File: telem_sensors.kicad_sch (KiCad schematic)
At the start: 29 parts, among them J4 Thermistor Molex, J6 Thermistor Molex, J8 SMA, U10 MAX-M10S, U4 LSM6DSRXTR, U5 MCP6L01x-xLT, U7 BMP585, U8 MCP6L01x-xLT

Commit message: Updated Schematics & finished rev2 layout. Routing left
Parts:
- removed C21, C32, C33: 100nF, Capacitor_SMD:C_0603_1608Metric, symbol Device:C
- added C23, C25, C29: 100nF, Capacitor_SMD:C_0603_1608Metric, symbol Device:C
- C22, C24, C26, C27, C28, C30: Voltage Rating (none) -> 10V
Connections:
- net +1V8: now also C30.1
- net +3V3: now also C28.1, C23.1, C29.1; no longer C30.1
- net PGND: now also C23.2, C25.2, C29.2
- net THERM2: now also C25.1; no longer C28.1

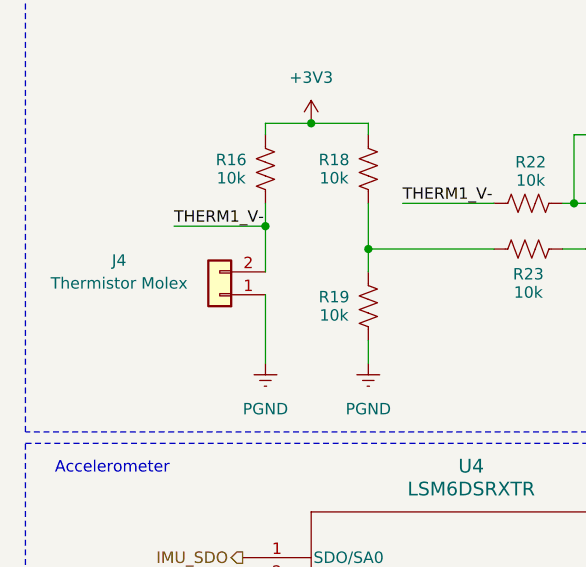
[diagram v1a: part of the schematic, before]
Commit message: Shrank board, updated all cap footprints. Updated thermistor headers to be vertical
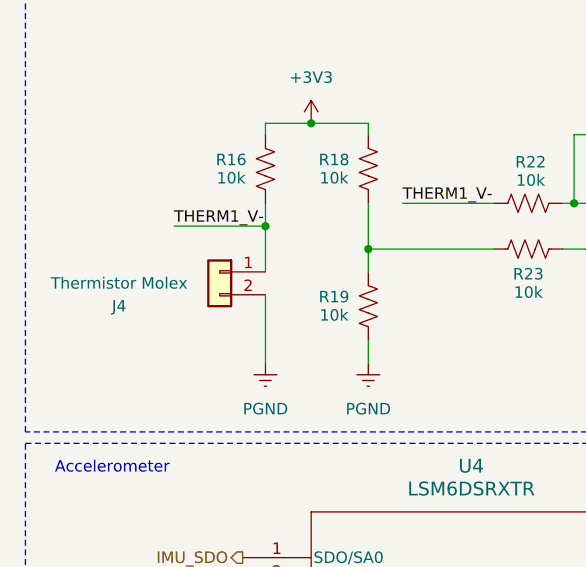
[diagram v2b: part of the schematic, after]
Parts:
- J4, J6: footprint Connector_Molex:Molex_MicroClasp_55935-0230_1x02_P2.00mm_Horizontal -> Connector_Molex:Molex_MicroClasp_55932-0230_1x02_P2.00mm_Vertical
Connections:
- net PGND: now also J4.2 (Pin_2); no longer J4.1 (Pin_1)
- net THERM1_V-: now also J4.1 (Pin_1); no longer J4.2 (Pin_2)
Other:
- moved on the sheet: J4
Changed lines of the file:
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@@
 	(wire
 		(pts
-			(xy 114.3 138.43) (xy 118.11 138.43)
+			(xy 73.66 58.42) (xy 73.66 66.04)
 		)
 		(stroke
@@
 	(wire
 		(pts
-			(xy 62.23 138.43) (xy 58.42 138.43)
+			(xy 114.3 138.43) (xy 118.11 138.43)
 		)
 		(stroke
@@
 	(wire
 		(pts
-			(xy 106.68 53.34) (xy 109.22 53.34)
+			(xy 62.23 138.43) (xy 58.42 138.43)
 		)
 		(stroke
@@
 	(wire
 		(pts
-			(xy 114.3 135.89) (xy 118.11 135.89)
+			(xy 106.68 53.34) (xy 109.22 53.34)
 		)
 		(stroke
@@
 	(wire
 		(pts
-			(xy 133.35 40.64) (xy 133.35 50.8)
+			(xy 114.3 135.89) (xy 118.11 135.89)
 		)
 		(stroke
@@
 	(wire
 		(pts
-			(xy 78.74 39.37) (xy 85.09 39.37)
+			(xy 133.35 40.64) (xy 133.35 50.8)
 		)
 		(stroke
@@
 	(wire
 		(pts
-			(xy 127 135.89) (xy 124.46 135.89)
+			(xy 78.74 39.37) (xy 85.09 39.37)
 		)
 		(stroke
@@
 	(wire
 		(pts
-			(xy 208.28 121.92) (xy 209.55 121.92)
+			(xy 127 135.89) (xy 124.46 135.89)
 		)
 		(stroke
@@
 	(wire
 		(pts
-			(xy 73.66 58.42) (xy 73.66 66.04)
+			(xy 208.28 121.92) (xy 209.55 121.92)
 		)
 		(stroke
@@
 	(symbol
 		(lib_id "Connector_Generic:Conn_01x02")
-		(at 68.58 58.42 180)
+		(at 68.58 55.88 0)
+		(mirror y)
 		(unit 1)
 		(body_style 1)
@@
 		(dnp no)
 		(property "Reference" "J4"
-			(at 57.404 54.61 0)
+			(at 57.404 59.69 0)
 			(show_name no)
 			(do_not_autoplace no)
@@
 			)
 		)
-		(property "Footprint" "Connector_Molex:Molex_MicroClasp_55935-0230_1x02_P2.00mm_Horizontal"
-			(at 68.58 58.42 0)
+		(property "Footprint" "Connector_Molex:Molex_MicroClasp_55932-0230_1x02_P2.00mm_Vertical"
+			(at 68.58 55.88 0)
 			(hide yes)
 			(show_name no)
@@
 		)
 		(property "Datasheet" ""
-			(at 68.58 58.42 0)
+			(at 68.58 55.88 0)
 			(hide yes)
 			(show_name no)
@@
 		)
 		(property "Description" "Generic connector, single row, 01x02, script generated (kicad-library-utils/schlib/autogen/connector/)"
-			(at 68.58 58.42 0)
+			(at 68.58 55.88 0)
 			(hide yes)
 			(show_name no)
@@
 			)
 		)
-		(property "Footprint" "Connector_Molex:Molex_MicroClasp_55935-0230_1x02_P2.00mm_Horizontal"
+		(property "Footprint" "Connector_Molex:Molex_MicroClasp_55932-0230_1x02_P2.00mm_Vertical"
 			(at 168.91 53.34 0)
 			(hide yes)
